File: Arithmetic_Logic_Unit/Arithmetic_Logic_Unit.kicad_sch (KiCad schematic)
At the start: 1 part, among them J1 PC104

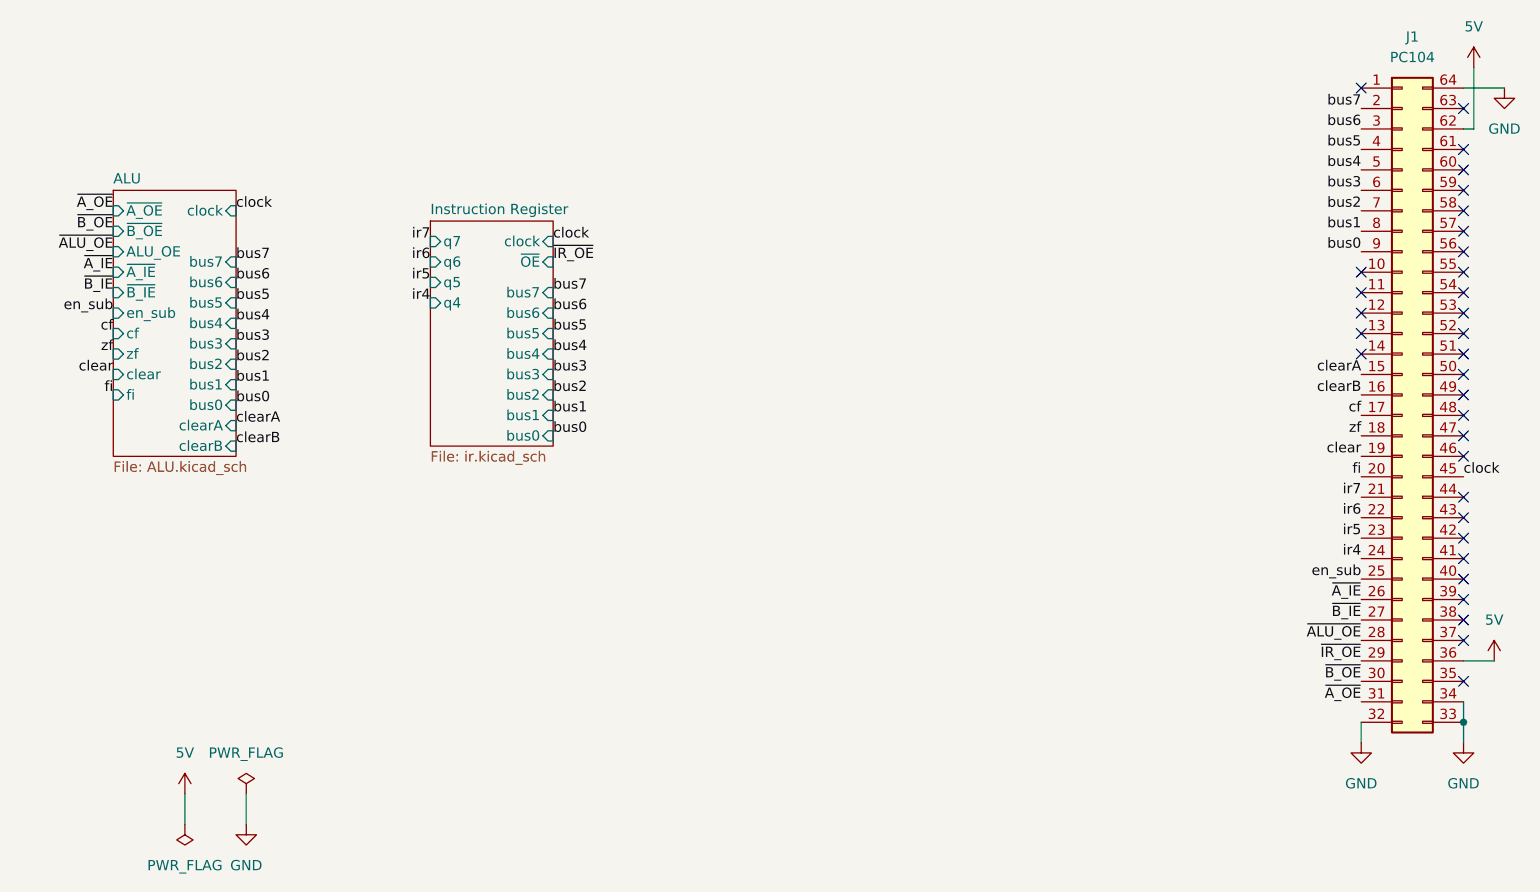
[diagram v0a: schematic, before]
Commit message: added bypass capacitors
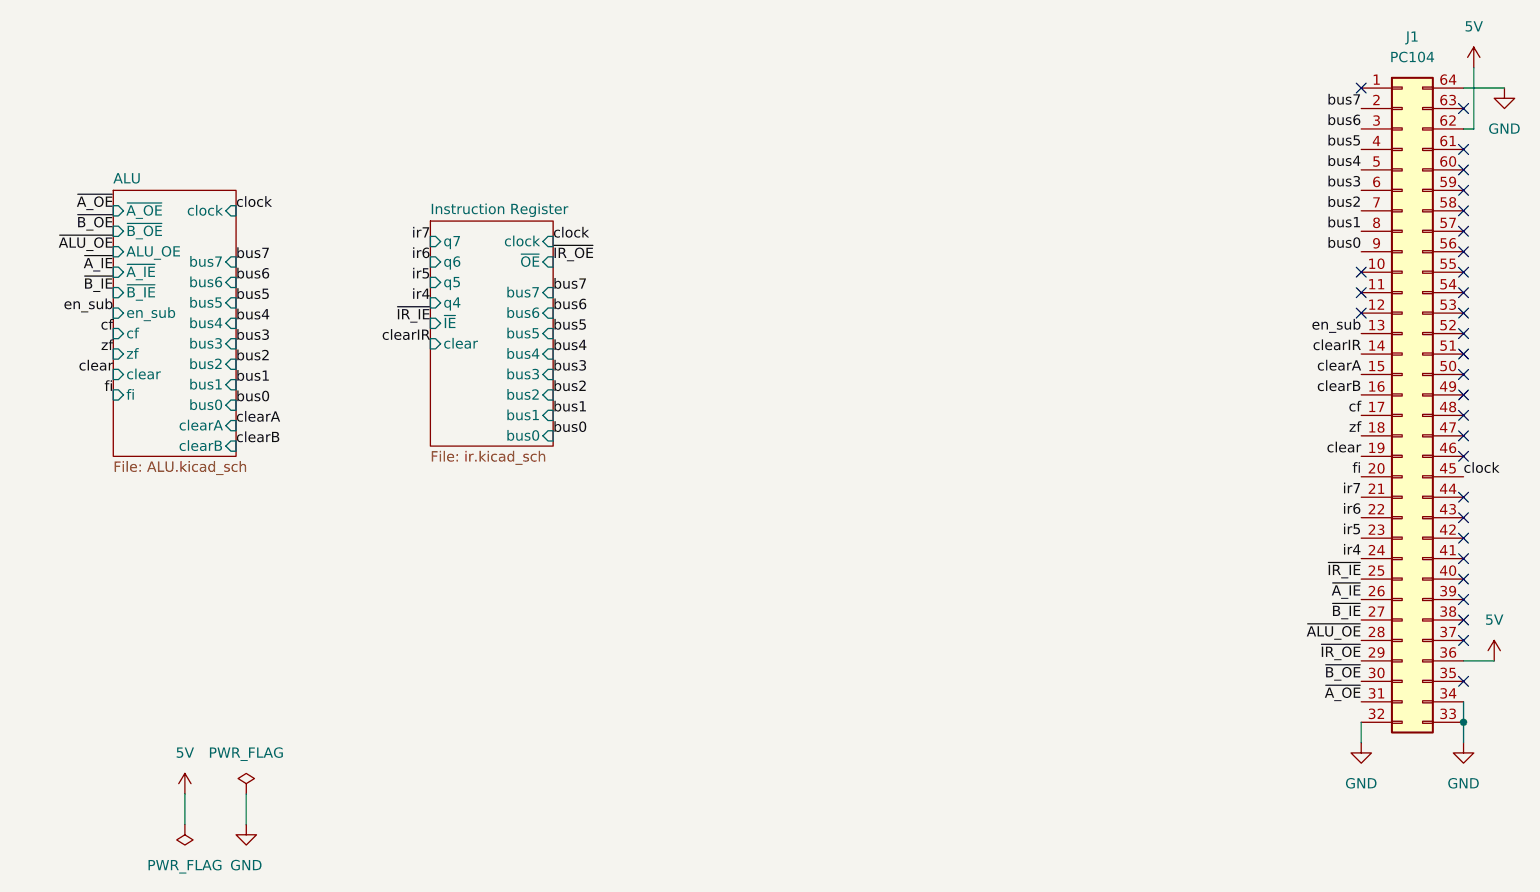
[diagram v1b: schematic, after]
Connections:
- net en_sub: now also J1.13 (Pin_13); no longer J1.25 (Pin_25)
- net clearIR: now reaches J1.14 (Pin_14)
- new net ~{IR_IE}: J1.25 (Pin_25)
- no-connect marks 32 -> 30
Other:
- sheet Instruction Register ports: added clear, ~{IE}; removed none
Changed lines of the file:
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@@
-	)
-	(no_connect
-		(at 250.19 58.42)
 	)
 	(no_connect
@@
 	(no_connect
 		(at 262.89 50.8)
-	)
-	(no_connect
-		(at 250.19 60.96)
 	)
 	(no_connect
@@
 		)
 	)
+	(label "clearIR"
+		(at 250.19 60.96 180)
+		(fields_autoplaced yes)
+		(effects
+			(font
+				(size 1.27 1.27)
+			)
+			(justify right bottom)
+		)
+	)
 	(label "bus5"
 		(at 149.86 58.42 0)
@@
 		)
 	)
+	(label "~{IR_IE}"
+		(at 250.19 88.9 180)
+		(fields_autoplaced yes)
+		(effects
+			(font
+				(size 1.27 1.27)
+			)
+			(justify right bottom)
+		)
+	)
 	(label "bus1"
 		(at 110.49 64.77 0)
@@
 		)
 	)
+	(label "clearIR"
+		(at 134.62 59.69 180)
+		(fields_autoplaced yes)
+		(effects
+			(font
+				(size 1.27 1.27)
+			)
+			(justify right bottom)
+		)
+	)
+	(label "en_sub"
+		(at 250.19 58.42 180)
+		(fields_autoplaced yes)
+		(effects
+			(font
+				(size 1.27 1.27)
+			)
+			(justify right bottom)
+		)
+	)
 	(label "~{B_IE}"
 		(at 95.25 53.34 180)
@@
 		)
 	)
-	(label "en_sub"
-		(at 250.19 88.9 180)
+	(label "~{IR_IE}"
+		(at 134.62 57.15 180)
 		(fields_autoplaced yes)
 		(effects
@@
 			)
 		)
+		(pin "~{IE}" input
+			(at 134.62 57.15 180)
+			(effects
+				(font
+					(size 1.27 1.27)
+				)
+				(justify left)
+			)
+		)
+		(pin "clear" input
+			(at 134.62 59.69 180)
+			(effects
+				(font
+					(size 1.27 1.27)
+				)
+				(justify left)
+			)
+		)

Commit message: layed out PCB
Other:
- removed sheet Instruction Register
